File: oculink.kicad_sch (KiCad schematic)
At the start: 0 parts

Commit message: [#56643] Create buses for interfaces, assign buses to blocks
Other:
- company: (none) -> Antmicro Ltd.
- title: (none) -> Com Express 7 baseboard
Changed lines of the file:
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@@
 (kicad_sch (version 20230121) (generator eeschema)
-  (paper "A4")
+  (paper "A3")
+  (title_block
+    (title "Com Express 7 baseboard")
+    (date "2024-03-22")
+    (rev "1.0.0")
+    (company "Antmicro Ltd.")
+  )
   (hierarchical_label "PCIe_x8{PCIe}" (shape input) (at 251.46 68.58 0) (fields_autoplaced)
     (effects (font (size 1.27 1.27)) (justify left))

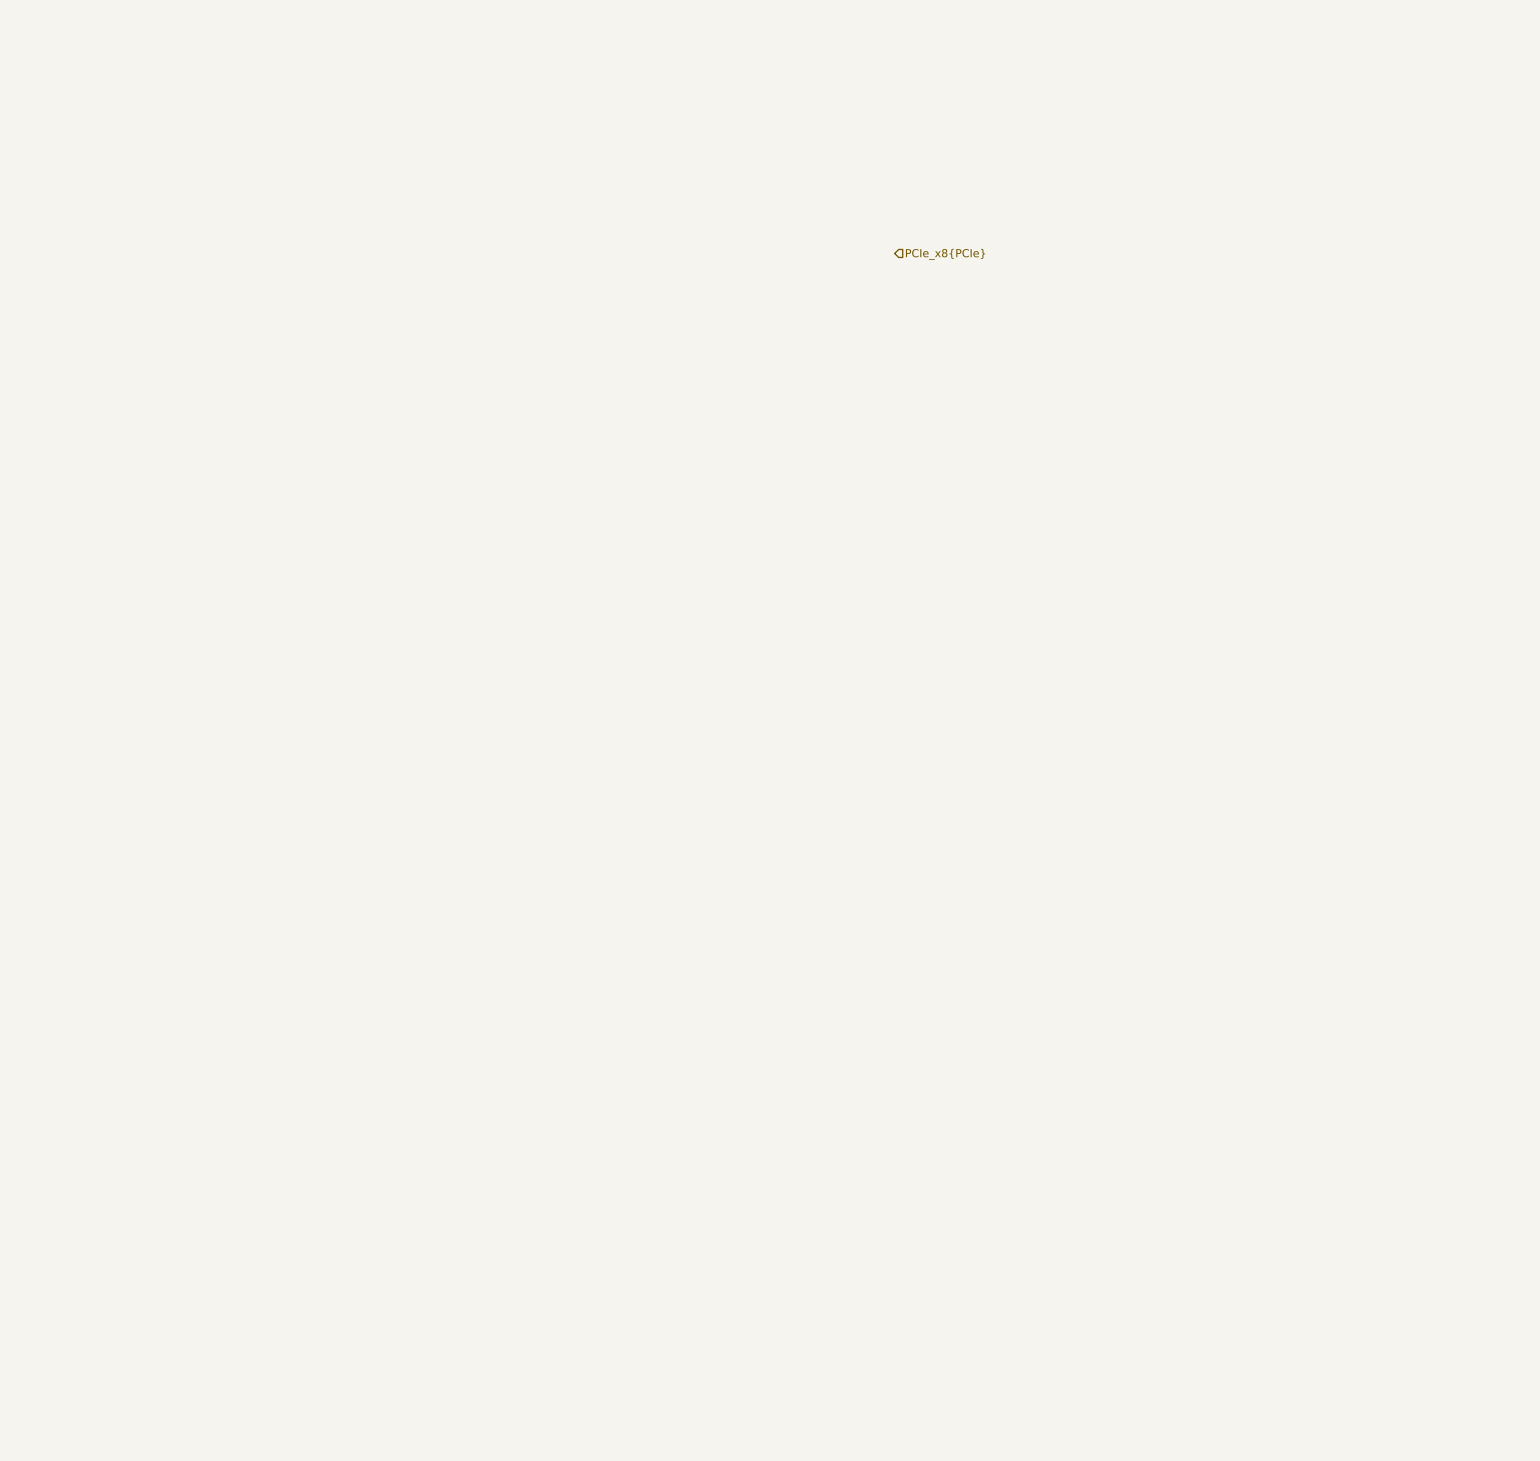
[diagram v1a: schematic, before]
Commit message: [#57056] Create schematics for M.2 and OCuLink connectors
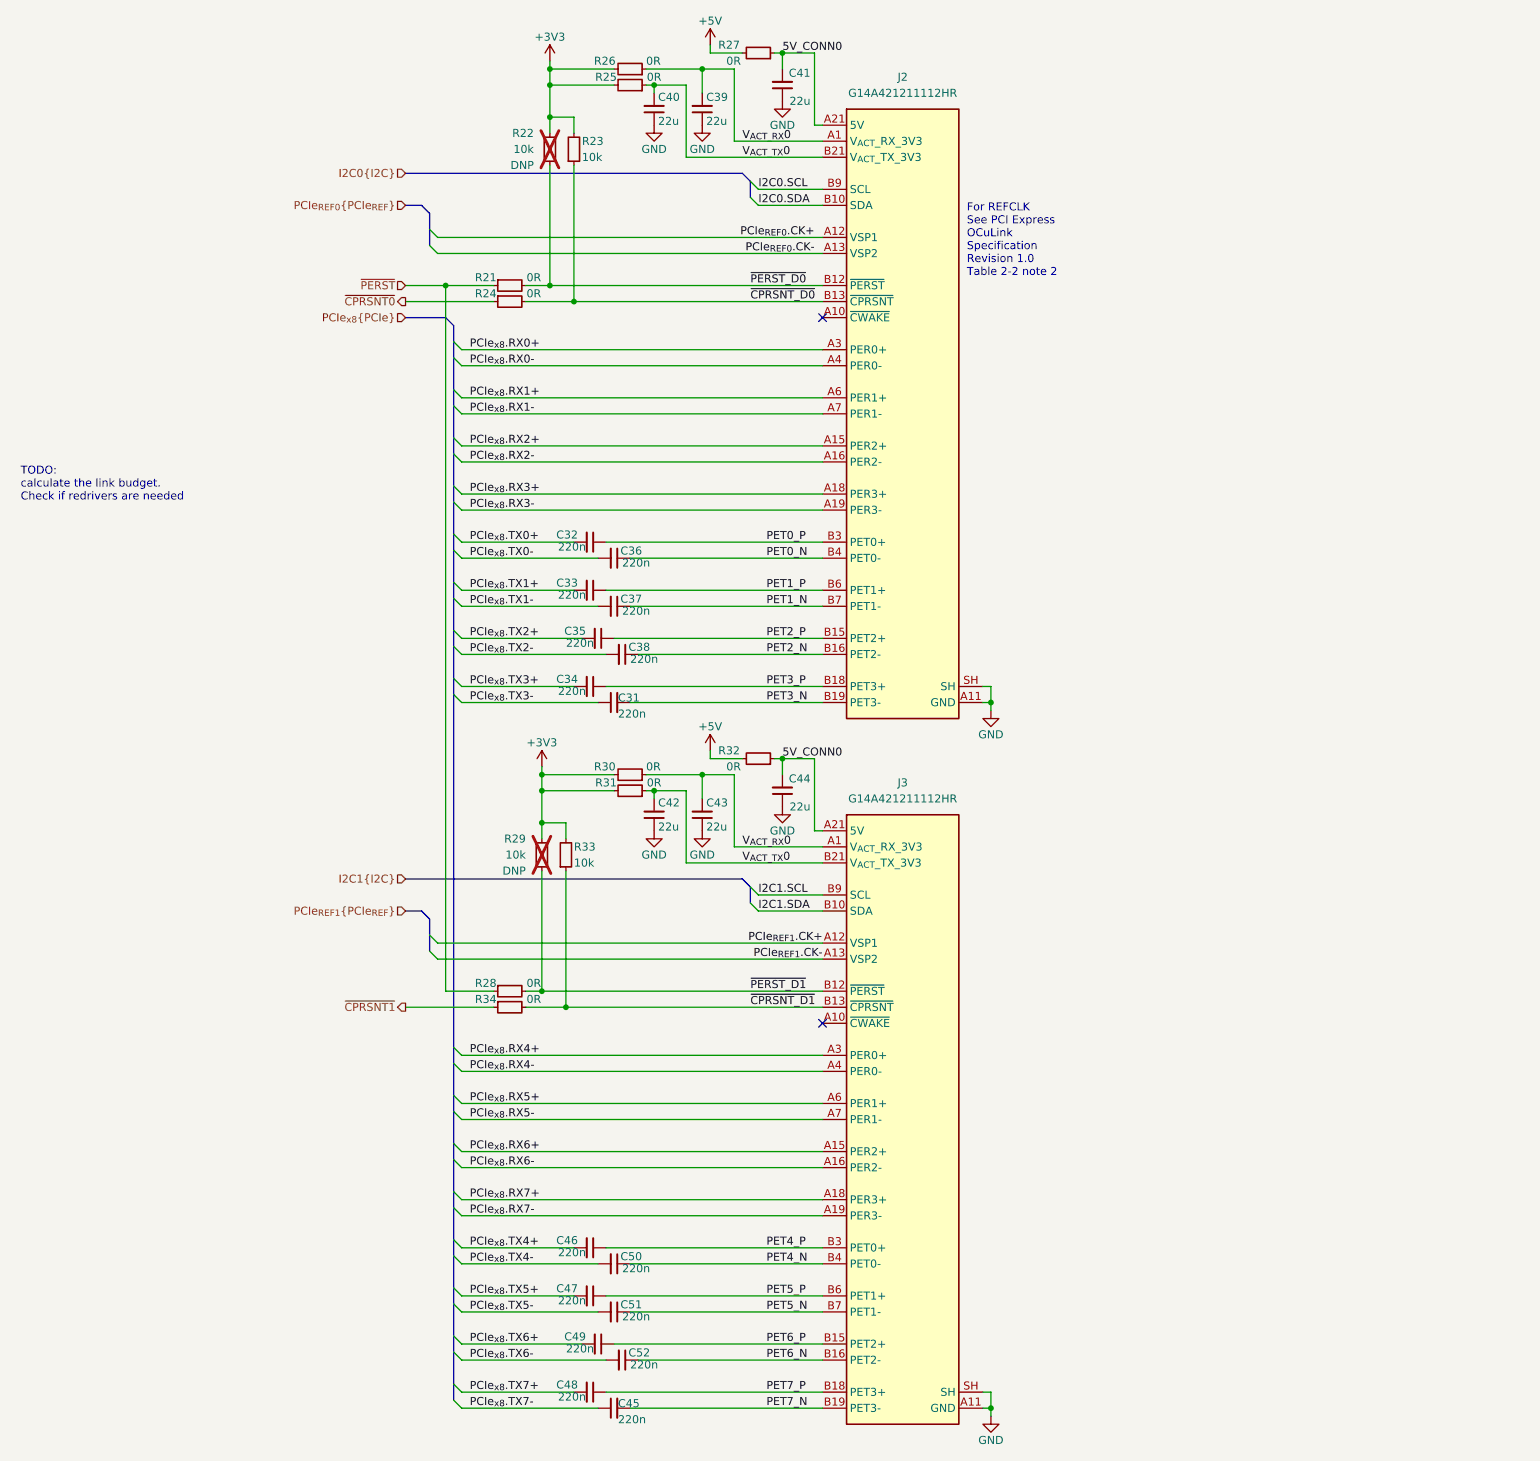
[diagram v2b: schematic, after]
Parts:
- added C31, C32, C33, C34, C35, C36, C37, C38, C45, C46, C47, C48, C49, C50, C51, C52: C_220n_0402, antmicro-footprints:C_0402_1005Metric, symbol antmicroCapacitors0402:C_220n_0402
- added C39, C40, C41, C42, C43, C44: C_22u_0603, antmicro-footprints:C_0603_1608Metric, symbol antmicroCapacitors0603:C_22u_0603
- added J2, J3: OCuLink_x4_Amphenol_G14A421211112HR, antmicro-footprints:Amphenol_G14A421211112HR, symbol antmicroPciConnectors:OCuLink_x4_Amphenol_G14A421211112HR
- added R21, R24, R25, R26, R28, R30, R31, R34: R_0R_0402, antmicro-footprints:R_0402_1005Metric, symbol antmicroResistors0402:R_0R_0402
- added R22, R23, R29, R33: R_10k_0402, antmicro-footprints:R_0402_1005Metric, symbol antmicroResistors0402:R_10k_0402
- added R27, R32: R_0R_0603, antmicro-footprints:R_0603_1608Metric, symbol antmicroResistors0603:R_0R_0603
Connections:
- new net +3V3: R22.2, R23.2, R25.2, R26.2, R29.2, R30.2, R31.2, R33.2
- new net +5V: R27.2, R32.2
- new net 5V_CONN0: C41.2, C44.2, J2.A21 (5V), J2.B1 (5V), J3.A21 (5V), J3.B1 (5V), R27.1, R32.1
- new net GND: C39.1, C40.1, C41.1, C42.1, C43.1, C44.1, J2.A11 (GND), J2.A14 (GND), J2.A17 (GND), J2.A2 (GND), J2.A20 (GND), J2.A5 (GND), J2.A8 (GND), J2.B11 (GND), J2.B14 (GND), J2.B17 (GND), J2.B2 (GND), J2.B20 (GND), J2.B5 (GND), J2.B8 (GND), J2.SH, J3.A11 (GND), J3.A14 (GND), J3.A17 (GND), J3.A2 (GND), J3.A20 (GND), J3.A5 (GND), J3.A8 (GND), J3.B11 (GND), J3.B14 (GND), J3.B17 (GND), J3.B2 (GND), J3.B20 (GND), J3.B5 (GND), J3.B8 (GND), J3.SH
- new net I2C0.SCL: J2.B9 (SCL)
- new net I2C0.SDA: J2.B10 (SDA)
- new net I2C1.SCL: J3.B9 (SCL)
- new net I2C1.SDA: J3.B10 (SDA)
- new net PCIe_{REF0}.CK+: J2.A12 (VSP1)
- new net PCIe_{REF0}.CK-: J2.A13 (VSP2)
- new net PCIe_{REF1}.CK+: J3.A12 (VSP1)
- new net PCIe_{REF1}.CK-: J3.A13 (VSP2)
- new net PCIe_{x8}.RX0+: J2.A3 (PER0+)
- new net PCIe_{x8}.RX0-: J2.A4 (PER0-)
- new net PCIe_{x8}.RX1+: J2.A6 (PER1+)
- new net PCIe_{x8}.RX1-: J2.A7 (PER1-)
- new net PCIe_{x8}.RX2+: J2.A15 (PER2+)
- new net PCIe_{x8}.RX2-: J2.A16 (PER2-)
- new net PCIe_{x8}.RX3+: J2.A18 (PER3+)
- new net PCIe_{x8}.RX3-: J2.A19 (PER3-)
- new net PCIe_{x8}.RX4+: J3.A3 (PER0+)
- new net PCIe_{x8}.RX4-: J3.A4 (PER0-)
- new net PCIe_{x8}.RX5+: J3.A6 (PER1+)
- new net PCIe_{x8}.RX5-: J3.A7 (PER1-)
- new net PCIe_{x8}.RX6+: J3.A15 (PER2+)
- new net PCIe_{x8}.RX6-: J3.A16 (PER2-)
- new net PCIe_{x8}.RX7+: J3.A18 (PER3+)
- new net PCIe_{x8}.RX7-: J3.A19 (PER3-)
- new net PCIe_{x8}.TX0+: C32.2
- new net PCIe_{x8}.TX0-: C36.2
- new net PCIe_{x8}.TX1+: C33.2
- new net PCIe_{x8}.TX1-: C37.2
- new net PCIe_{x8}.TX2+: C35.2
- new net PCIe_{x8}.TX2-: C38.2
- new net PCIe_{x8}.TX3+: C34.2
- new net PCIe_{x8}.TX3-: C31.1
- new net PCIe_{x8}.TX4+: C46.2
- new net PCIe_{x8}.TX4-: C50.2
- new net PCIe_{x8}.TX5+: C47.2
- new net PCIe_{x8}.TX5-: C51.2
- new net PCIe_{x8}.TX6+: C49.2
- new net PCIe_{x8}.TX6-: C52.2
- new net PCIe_{x8}.TX7+: C48.2
- new net PCIe_{x8}.TX7-: C45.1
- new net PET0_N: C36.1, J2.B4 (PET0-)
- new net PET0_P: C32.1, J2.B3 (PET0+)
- new net PET1_N: C37.1, J2.B7 (PET1-)
- new net PET1_P: C33.1, J2.B6 (PET1+)
- new net PET2_N: C38.1, J2.B16 (PET2-)
- new net PET2_P: C35.1, J2.B15 (PET2+)
- new net PET3_N: C31.2, J2.B19 (PET3-)
- new net PET3_P: C34.1, J2.B18 (PET3+)
- new net PET4_N: C50.1, J3.B4 (PET0-)
- new net PET4_P: C46.1, J3.B3 (PET0+)
- new net PET5_N: C51.1, J3.B7 (PET1-)
- new net PET5_P: C47.1, J3.B6 (PET1+)
- new net PET6_N: C52.1, J3.B16 (PET2-)
- new net PET6_P: C49.1, J3.B15 (PET2+)
- new net PET7_N: C45.2, J3.B19 (PET3-)
- new net PET7_P: C48.1, J3.B18 (PET3+)
- new net V_{ACT_RX}0: C39.2, C43.2, J2.A1 (V_{ACT}_RX_3V3), J3.A1 (V_{ACT}_RX_3V3), R26.1, R30.1
- new net V_{ACT_TX}0: C40.2, C42.2, J2.B21 (V_{ACT}_TX_3V3), J3.B21 (V_{ACT}_TX_3V3), R25.1, R31.1
- new net ~{CPRSNT0}: R24.1
- new net ~{CPRSNT1}: R34.1
- new net ~{CPRSNT_D0}: J2.B13 (~{CPRSNT}), R23.1, R24.2
- new net ~{CPRSNT_D1}: J3.B13 (~{CPRSNT}), R33.1, R34.2
- new net ~{PERST_D0}: J2.B12 (~{PERST}), R21.2, R22.1
- new net ~{PERST_D1}: J3.B12 (~{PERST}), R28.2, R29.1
- new net ~{PERST}: R21.1, R28.1
- no-connect marks 0 -> 2
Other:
- note added: "For REFCLK See PCI Express OCuLink Specification Revision 1.0 Table 2-2 note 2"
- note added: "TODO: calculate the link budget. Check if redrivers are needed"

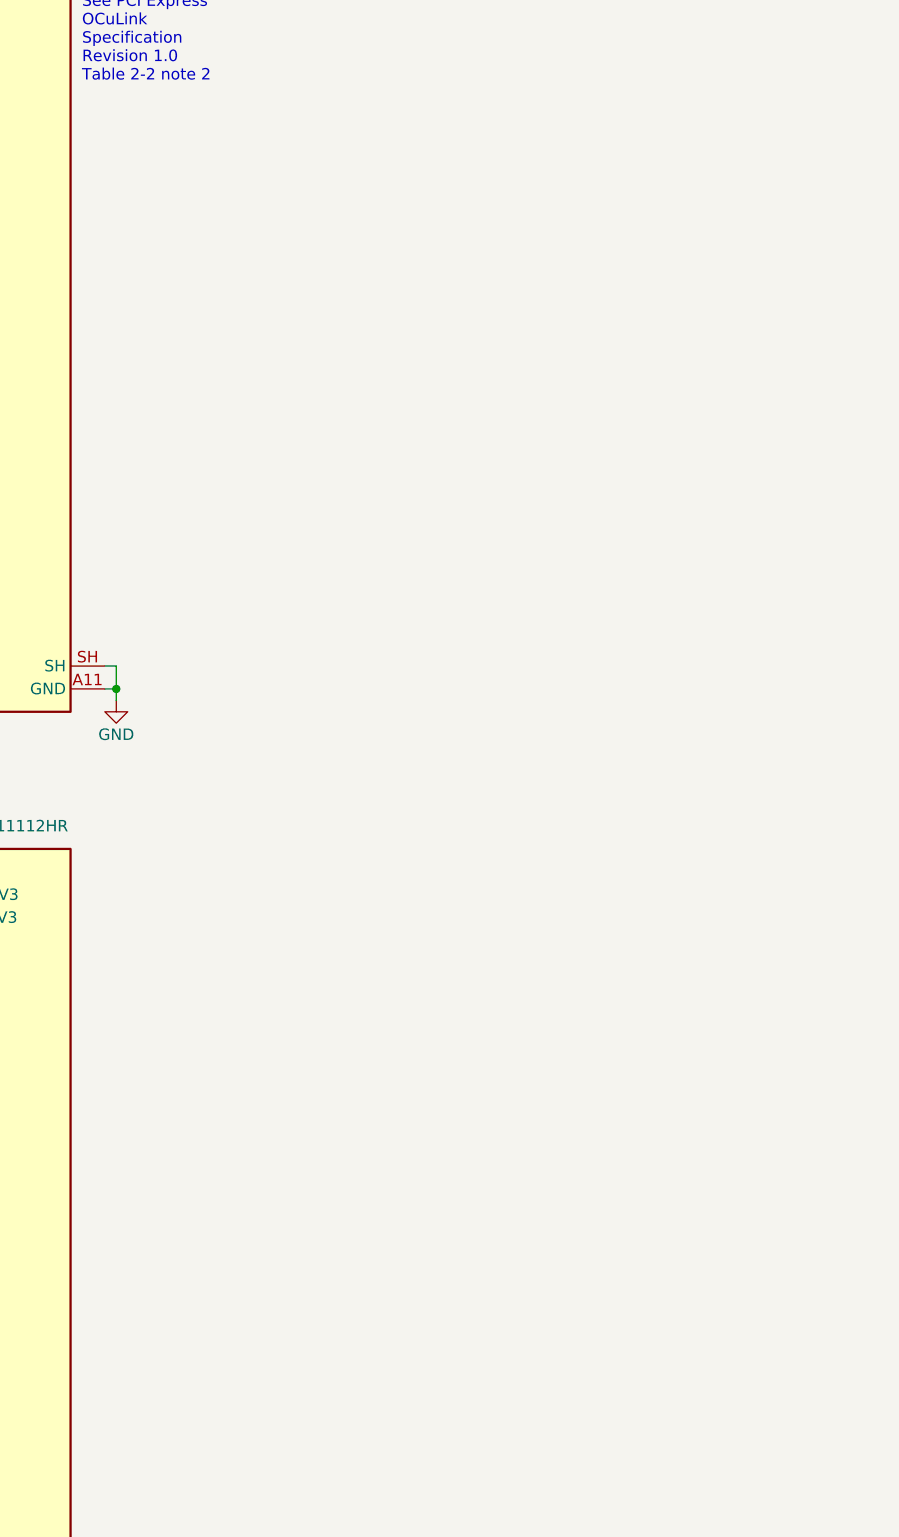
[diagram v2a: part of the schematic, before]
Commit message: [#57056] Add ESD diodes to OCuLink
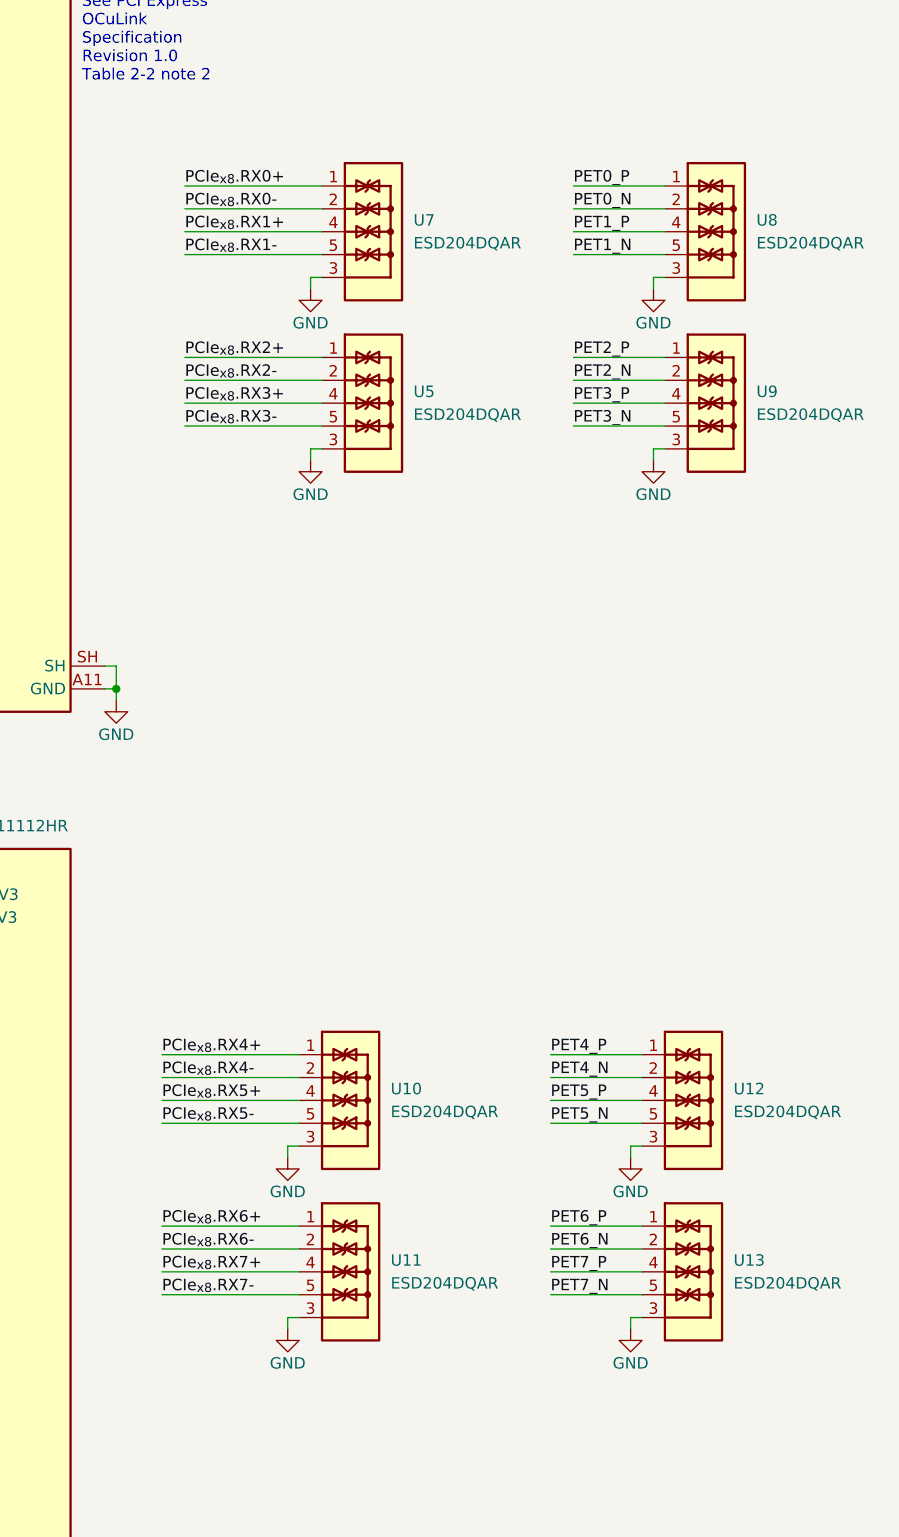
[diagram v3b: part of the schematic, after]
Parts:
- added U10, U11, U12, U13, U5, U7, U8, U9: ESD204DQAR, antmicro-footprints:USON-10_2.5x1mm_P0.5mm, symbol antmicroTVSDiodes:ESD204DQAR
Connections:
- net GND: now also U10.3, U10.8, U11.3, U11.8, U12.3, U12.8, U13.3, U13.8, U5.3, U5.8, U7.3, U7.8, U8.3, U8.8, U9.3, U9.8
- net PCIe_{x8}.RX0+: now also U7.1, U7.10
- net PCIe_{x8}.RX0-: now also U7.2, U7.9
- net PCIe_{x8}.RX1+: now also U7.4, U7.7
- net PCIe_{x8}.RX1-: now also U7.5, U7.6
- net PCIe_{x8}.RX2+: now also U5.1, U5.10
- net PCIe_{x8}.RX2-: now also U5.2, U5.9
- net PCIe_{x8}.RX3+: now also U5.4, U5.7
- net PCIe_{x8}.RX3-: now also U5.5, U5.6
- net PCIe_{x8}.RX4+: now also U10.1, U10.10
- net PCIe_{x8}.RX4-: now also U10.2, U10.9
- net PCIe_{x8}.RX5+: now also U10.4, U10.7
- net PCIe_{x8}.RX5-: now also U10.5, U10.6
- net PCIe_{x8}.RX6+: now also U11.1, U11.10
- net PCIe_{x8}.RX6-: now also U11.2, U11.9
- net PCIe_{x8}.RX7+: now also U11.4, U11.7
- net PCIe_{x8}.RX7-: now also U11.5, U11.6
- net PET0_N: now also U8.2, U8.9
- net PET0_P: now also U8.1, U8.10
- net PET1_N: now also U8.5, U8.6
- net PET1_P: now also U8.4, U8.7
- net PET2_N: now also U9.2, U9.9
- net PET2_P: now also U9.1, U9.10
- net PET3_N: now also U9.5, U9.6
- net PET3_P: now also U9.4, U9.7
- net PET4_N: now also U12.2, U12.9
- net PET4_P: now also U12.1, U12.10
- net PET5_N: now also U12.5, U12.6
- net PET5_P: now also U12.4, U12.7
- net PET6_N: now also U13.2, U13.9
- net PET6_P: now also U13.1, U13.10
- net PET7_N: now also U13.5, U13.6
- net PET7_P: now also U13.4, U13.7
